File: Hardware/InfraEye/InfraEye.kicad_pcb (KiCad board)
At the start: 2 copper layers, 1 part, among them J1 Conn_02x02_Top_Bottom

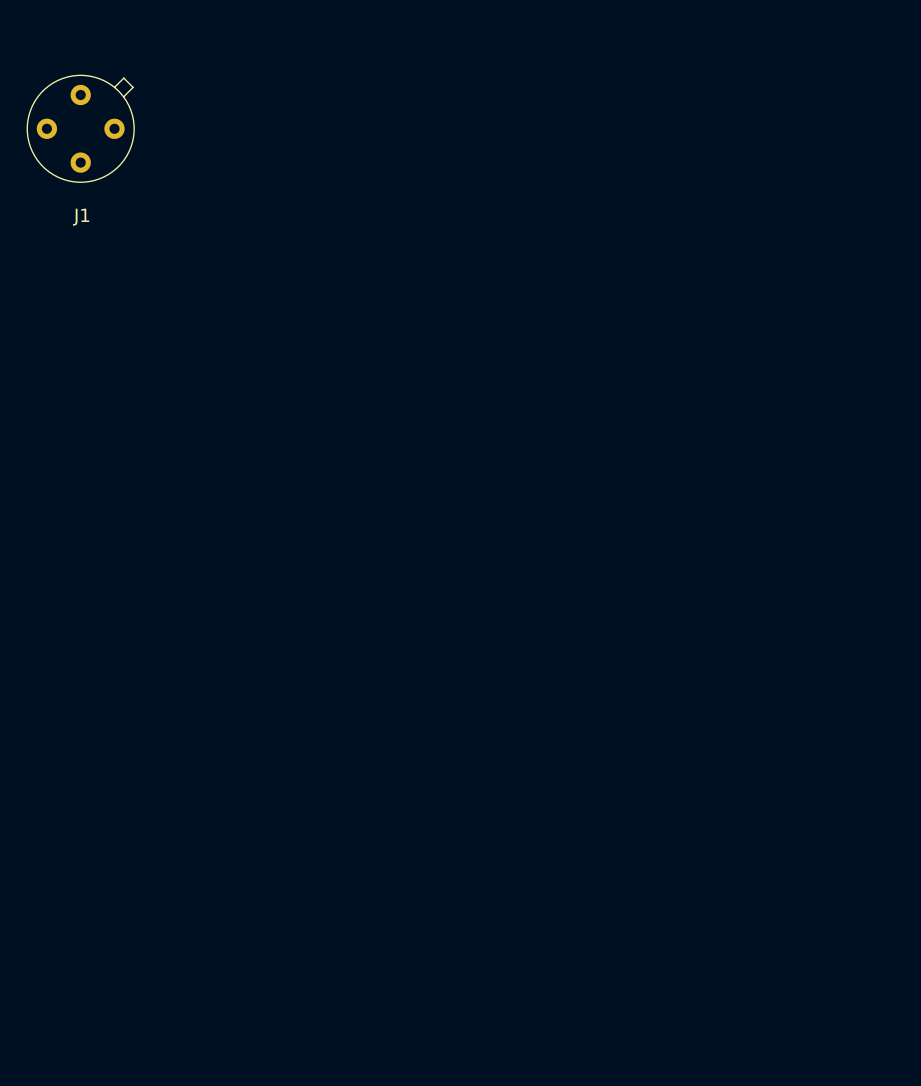
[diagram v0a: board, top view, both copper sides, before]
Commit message: Added footprints for LCD, ESP32 board and IR sensor
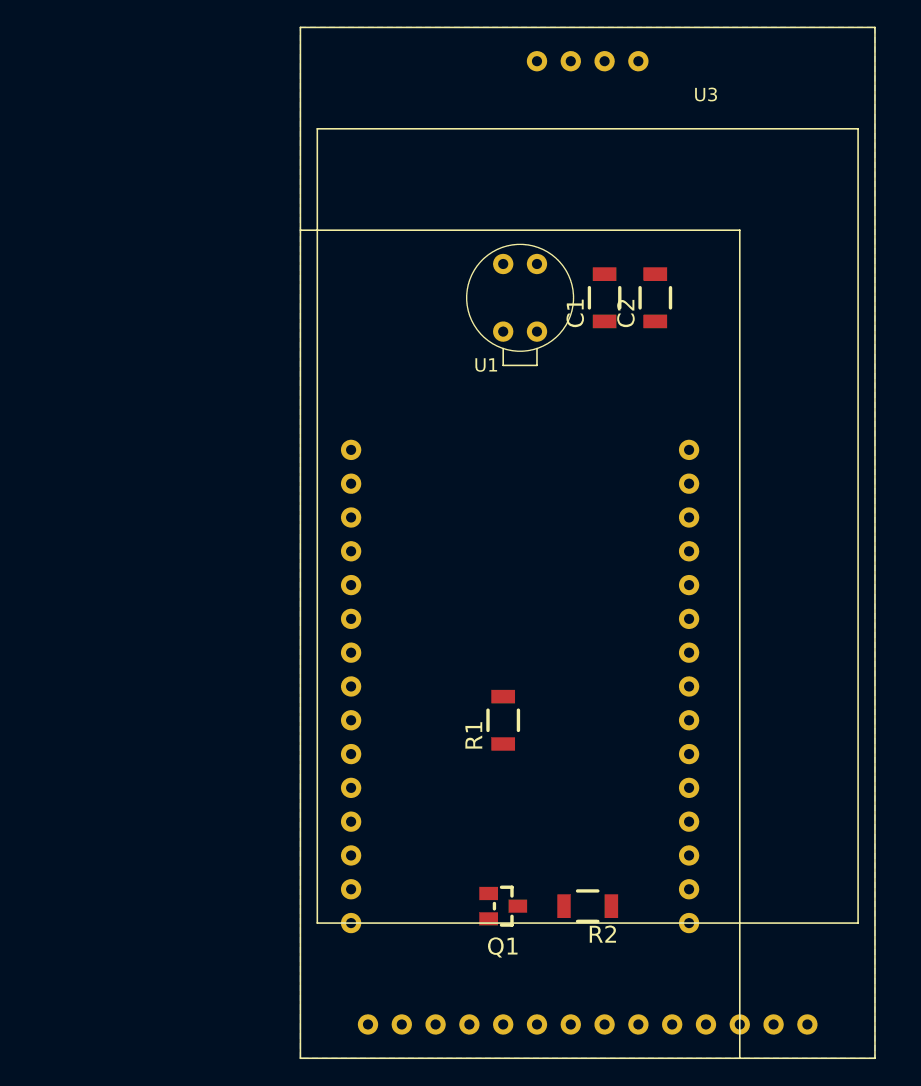
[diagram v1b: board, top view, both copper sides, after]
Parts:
- removed J1: Conn_02x02_Top_Bottom, OLIMEX_IC-FP:MLX90614
- added C1: 10nF, OLIMEX_RLC-FP:C_1206_5MIL_DWS_ISO, F.Cu at (129.5, 61.0)
- added C2: 100nF, OLIMEX_RLC-FP:C_1206_5MIL_DWS_ISO, F.Cu at (133.3, 61.0)
- added Q1: Q_NPN_BCE, OLIMEX_Diodes-FP:SOT23-3, F.Cu at (121.9, 106.7)
- added R1: R, OLIMEX_RLC-FP:R_1206_5MIL_DWS_ISO, F.Cu at (121.9, 92.7)
- added R2: R, OLIMEX_RLC-FP:R_1206_5MIL_DWS_ISO, F.Cu at (128.3, 106.7)
- added U1: MLX90640, InfraEye:MLX90614, F.Cu at (124.5, 63.5)
- added U2: ESP32-WROOM-32, InfraEye:ESP32-WROOM-32-30pin, B.Cu at (137.2, 66.0)
- added U3: TFT_SPI_24_LCD, InfraEye:TFT_LCD_24, F.Cu at (106.7, 40.6)
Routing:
- added copper zone on B.Cu, net GND

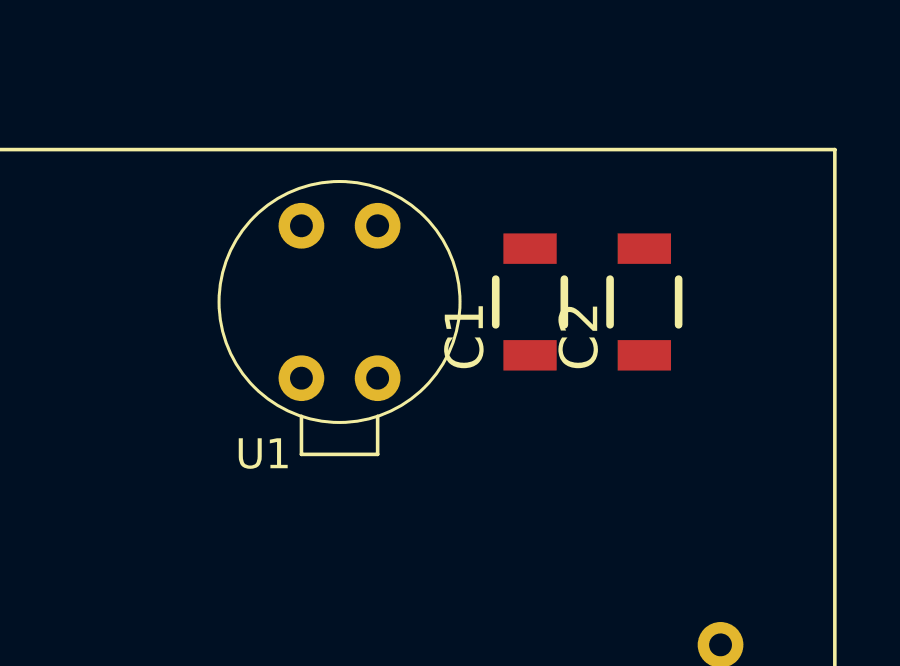
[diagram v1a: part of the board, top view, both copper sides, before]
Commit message: Fixed footprint for IR sensor (pins were mirrored as if sensor was mounted on other side of PCB)
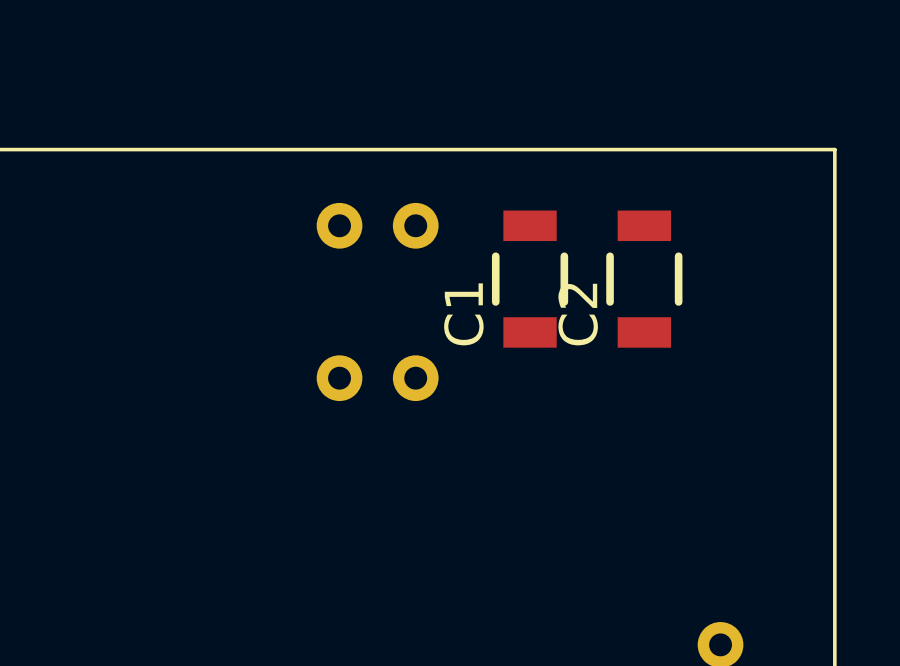
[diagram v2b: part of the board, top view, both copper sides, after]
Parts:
- U1: moved to B.Cu
- moved U1 1.27 mm to (123.2, 63.5), turned to 0 degrees
- moved C1 0.76 mm to (129.5, 60.2)
- moved C2 0.76 mm to (133.3, 60.2)
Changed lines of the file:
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@@
     (add_net "Net-(U3-Pad18)")
-  )
-  (module InfraEye:MLX90614 (layer F.Cu)
-    (at 124.46 63.5 180)
-    (fp_text reference U1 (at 3.81 -2.54) (layer F.SilkS)
-      (effects (font (size 1 1) (thickness 0.15)))
-    )
-    (fp_text value MLX90640 (at 1.27 -3.81) (layer F.Fab)
-      (effects (font (size 1 1) (thickness 0.15)))
-    )
-    (fp_circle (center 1.27 2.54) (end 5.08 3.81) (layer F.SilkS) (width 0.1))
-    (fp_line (start 0 -1.27) (end 0 -2.54) (layer F.SilkS) (width 0.12))
-    (fp_line (start 0 -2.54) (end 2.54 -2.54) (layer F.SilkS) (width 0.12))
-    (fp_line (start 2.54 -2.54) (end 2.54 -1.27) (layer F.SilkS) (width 0.12))
-    (pad 1 thru_hole circle (at 2.54 0 180) (size 1.524 1.524) (drill 0.762) (layers *.Cu *.Mask)
-      (net 1 "Net-(U1-Pad1)"))
-    (pad 2 thru_hole circle (at 2.54 5.08 180) (size 1.524 1.524) (drill 0.762) (layers *.Cu *.Mask)
-      (net 2 "Net-(C1-Pad1)"))
-    (pad 3 thru_hole circle (at 0 5.08 180) (size 1.524 1.524) (drill 0.762) (layers *.Cu *.Mask)
-      (net 3 GND))
-    (pad 4 thru_hole circle (at 0 0 180) (size 1.524 1.524) (drill 0.762) (layers *.Cu *.Mask)
-      (net 4 "Net-(U1-Pad4)"))
-    (model ${OLIMEXFOOTPATH}/OLIMEX_3Dmodels/MLX90614.step
-      (at (xyz 0 0 0))
-      (scale (xyz 1 1 1))
-      (rotate (xyz 0 0 -45))
-    )
   )
   (module InfraEye:TFT_LCD_24 (layer F.Cu)
@@
   )
   (module OLIMEX_RLC-FP:C_1206_5MIL_DWS_ISO (layer F.Cu)
-    (at 129.54 60.96 90)
+    (at 129.54 60.198 90)
     (attr smd)
     (fp_text reference C1 (at -1.143 -2.159 90) (layer F.SilkS)
@@
   )
   (module OLIMEX_RLC-FP:C_1206_5MIL_DWS_ISO (layer F.Cu)
-    (at 133.35 60.96 90)
+    (at 133.35 60.198 90)
     (attr smd)
     (fp_text reference C2 (at -1.143 -2.159 90) (layer F.SilkS)
@@
       (net 8 "Net-(U2-Pad30)"))
   )
+  (module InfraEye:MLX90614 (layer B.Cu)
+    (at 123.19 63.5)
+    (fp_text reference U1 (at 3.81 2.54) (layer B.SilkS)
+      (effects (font (size 1 1) (thickness 0.15)) (justify mirror))
+    )
+    (fp_text value MLX90640 (at 1.27 3.81) (layer B.Fab)
+      (effects (font (size 1 1) (thickness 0.15)) (justify mirror))
+    )
+    (fp_circle (center 1.27 -2.54) (end 5.08 -3.81) (layer B.SilkS) (width 0.1))
+    (fp_line (start 0 1.27) (end 0 2.54) (layer B.SilkS) (width 0.12))
+    (fp_line (start 0 2.54) (end 2.54 2.54) (layer B.SilkS) (width 0.12))
+    (fp_line (start 2.54 2.54) (end 2.54 1.27) (layer B.SilkS) (width 0.12))
+    (pad 1 thru_hole circle (at 0 0) (size 1.524 1.524) (drill 0.762) (layers *.Cu *.Mask)
+      (net 1 "Net-(U1-Pad1)"))
+    (pad 2 thru_hole circle (at 0 -5.08) (size 1.524 1.524) (drill 0.762) (layers *.Cu *.Mask)
+      (net 2 "Net-(C1-Pad1)"))
+    (pad 3 thru_hole circle (at 2.54 -5.08) (size 1.524 1.524) (drill 0.762) (layers *.Cu *.Mask)
+      (net 3 GND))
+    (pad 4 thru_hole circle (at 2.54 0) (size 1.524 1.524) (drill 0.762) (layers *.Cu *.Mask)
+      (net 4 "Net-(U1-Pad4)"))
+    (model ${OLIMEXFOOTPATH}/OLIMEX_3Dmodels/MLX90614.step
+      (at (xyz 0 0 0))
+      (scale (xyz 1 1 1))
+      (rotate (xyz 0 0 -45))
+    )
+  )
   (gr_line (start 139.7 55.88) (end 139.7 118.11) (layer F.SilkS) (width 0.12))
